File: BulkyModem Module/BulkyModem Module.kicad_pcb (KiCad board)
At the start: 2 copper layers, 100 x 100 mm, 81 parts, among them J1 DC IN, J2 DCE, J3 Module_Panel, J5 C64_Modem_IDC, K1 HK19F-DC, M1 Mounting, M2 Mounting, M3 Mounting, M4 Mounting, SW1 SET_1200, U1 74HCT244, U2 74HCT04, U3 MAX232, U4 MAX232, U5 74HCT04, U6 74HCT32

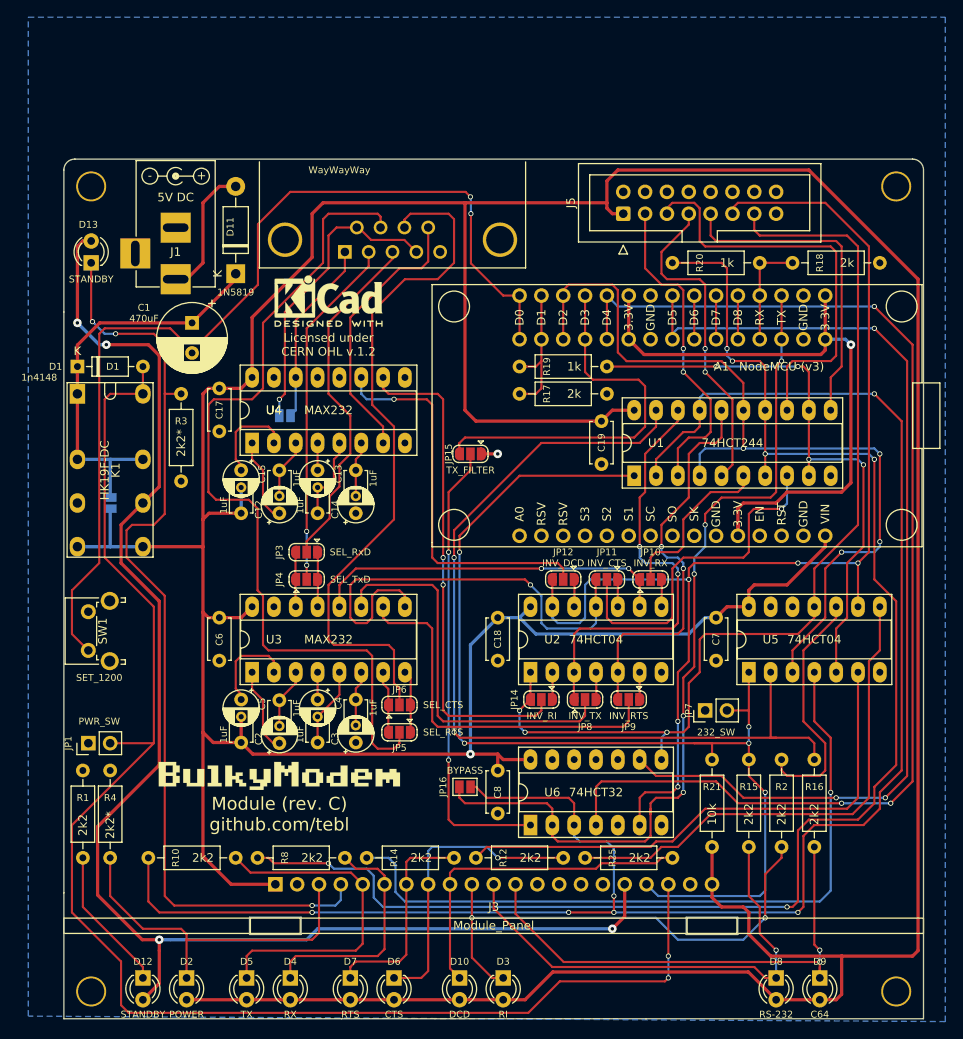
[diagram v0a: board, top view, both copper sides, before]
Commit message: Tweaks needed to make revision C actually work.
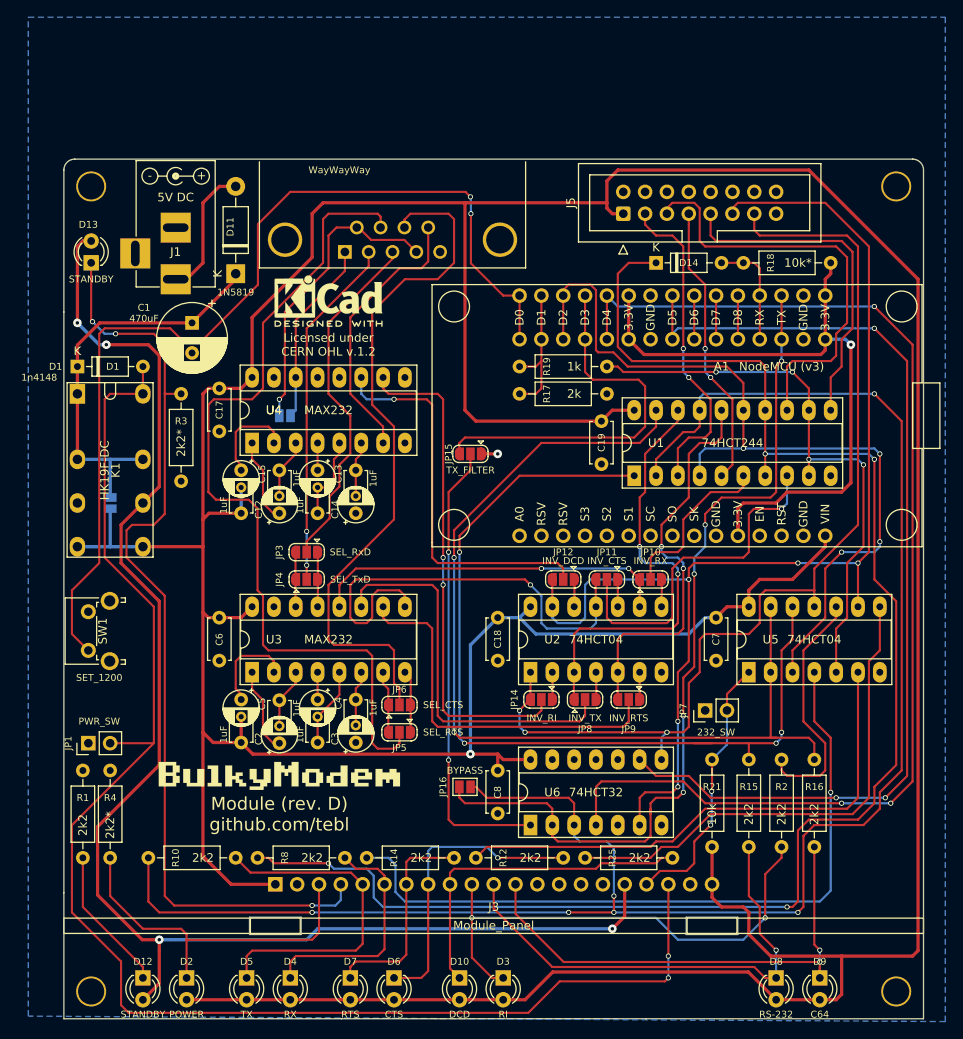
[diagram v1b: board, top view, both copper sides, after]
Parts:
- removed R20: 1k, resistor:R_Axial_DIN0207_L6.3mm_D2.5mm_P10.16mm_Horizontal
- added D14: 1N4148, Diode_THT:D_DO-35_SOD27_P7.62mm_Horizontal, F.Cu at (139.1, 66.7)
- R18: value 2k -> 10k*
- moved R18 5.72 mm to (159.4, 66.7)
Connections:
- J3 pad 18: MODE_232 -> MODE_SEL
- JP7 pad 2: MODE_232 -> MODE_SEL
- R18 pad 1: GND -> +3V3
- R21 pad 1: MODE_232 -> MODE_SEL
- U5 pad 1: MODE_232 -> MODE_SEL
- U5 pad 12: (no net) -> MODE_232
- U5 pad 13: GND -> MODE_C64
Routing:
- net MODE_SEL: track 0.00 -> 31.4 mm, vias 0 -> 2
- net MODE_232: track 128.1 -> 104.5 mm, vias 5 -> 4
- net ESP_RX: track 175.0 -> 184.8 mm, vias 6 -> 4
- net MODE_C64: track 106.5 -> 114.1 mm
- net /C64_RTS: track 38.0 -> 33.1 mm
- net +3V3: track 73.4 -> 77.4 mm
- net ESP_RI: track 116.3 -> 118.2 mm
- net /C64_CTS: track 37.9 -> 39.3 mm
- net /C64_RX: track 48.6 -> 50.0 mm
- net ESP_CTS: track 67.9 -> 66.8 mm
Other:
- board text added: "Module (rev. D) github.com/tebl"
- board text removed: "Module (rev. C) github.com/tebl"

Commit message: Upgrade to KiCAD8
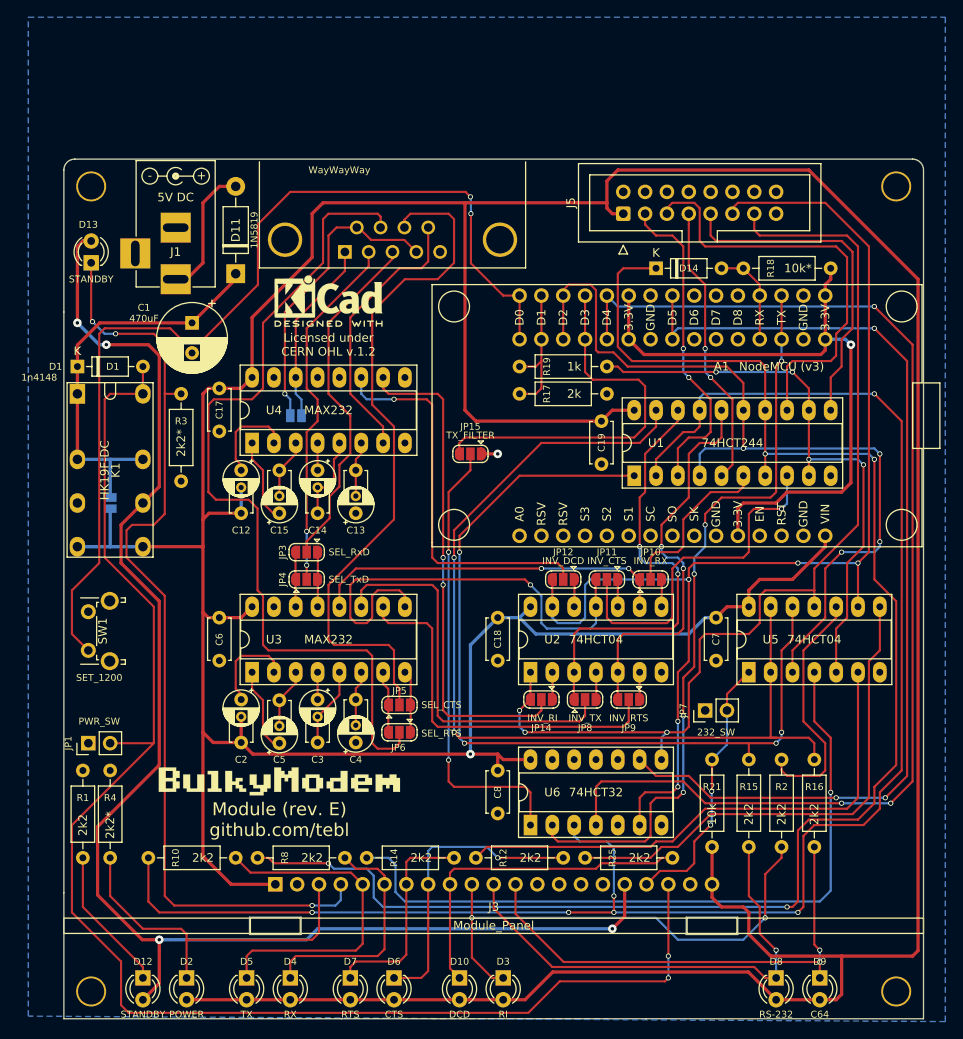
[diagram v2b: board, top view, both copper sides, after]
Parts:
- removed JP16: BYPASS, Jumper:SolderJumper-2_P1.3mm_Open_Pad1.0x1.5mm
- D11: footprint Diode_THT:D_DO-41_SOD81_P10.16mm_Horizontal -> BulkyModem:D_DO-41_SOD81_P10.16mm_Horizontal
- JP10, JP11, JP12, JP14, JP15, JP3, JP4, JP5, JP6, JP8, JP9: footprint Jumper:SolderJumper-3_P1.3mm_Open_RoundedPad1.0x1.5mm -> solder_bridge:SolderJumper-3_P1.3mm_Open_RoundedPad1.0x1.5mm
- JP13, JP2: footprint Jumper:SolderJumper-2_P1.3mm_Open_Pad1.0x1.5mm -> solder_bridge:SolderJumper-2_P1.3mm_Open_Pad1.0x1.5mm
- moved JP13 1.28 mm to (97.2, 84.5)
- moved D14 0.64 mm to (139.1, 67.3)
- moved G*** 0.64 mm to (95.2, 127.0)
- moved R18 0.64 mm to (159.4, 67.3)
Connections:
- net +3V3 renamed +3.3V
- net /ESP_DSR renamed /ESP_DSR_0
- net /ESP_DTR renamed /ESP_DTR_0
- A1 pad 1: (no net) -> unconnected-(A1-A0-Pad1)
- A1 pad 12: (no net) -> unconnected-(A1-EN-Pad12)
- A1 pad 13: (no net) -> unconnected-(A1-RST-Pad13)
- A1 pad 2: (no net) -> unconnected-(A1-RSV-Pad2)
- A1 pad 20: Net-(A1-Pad20) -> unconnected-(A1-D8-Pad20)_0
- A1 pad 3: (no net) -> unconnected-(A1-RSV-Pad3)
- A1 pad 4: (no net) -> unconnected-(A1-S3-Pad4)
- A1 pad 5: (no net) -> unconnected-(A1-S2-Pad5)
- A1 pad 6: (no net) -> unconnected-(A1-S1-Pad6)
- A1 pad 7: (no net) -> unconnected-(A1-SC-Pad7)
- A1 pad 8: (no net) -> unconnected-(A1-S0-Pad8)
- A1 pad 9: (no net) -> unconnected-(A1-SK-Pad9)
- C14 pad 1: Net-(C14-Pad1) -> unconnected-(U4-C2+-Pad4)
- C14 pad 2: Net-(C14-Pad2) -> unconnected-(U4-C2--Pad5)
- C15 pad 1: Net-(C15-Pad1) -> unconnected-(U4-C1+-Pad1)
- C15 pad 2: Net-(C15-Pad2) -> unconnected-(U4-C1--Pad3)
- C2 pad 1: Net-(C2-Pad1) -> unconnected-(U3-VS+-Pad2)
- C3 pad 1: Net-(C3-Pad1) -> unconnected-(U3-C2+-Pad4)
- C3 pad 2: Net-(C3-Pad2) -> unconnected-(U3-C2--Pad5)
- C4 pad 2: Net-(C4-Pad2) -> unconnected-(U3-VS--Pad6)
- C5 pad 1: Net-(C5-Pad1) -> unconnected-(U3-C1+-Pad1)
- C5 pad 2: Net-(C5-Pad2) -> unconnected-(U3-C1--Pad3)
- J5 pad 16: (no net) -> unconnected-(J5-N.C.-Pad16)
- J5 pad 8: (no net) -> unconnected-(J5-N.C-Pad8)
- K1 pad 6: (no net) -> unconnected-(K1-NC_1-Pad6)
- R12 pad 1: Net-(R12-Pad1) -> unconnected-(U5-Pad6)
- R14 pad 1: Net-(R14-Pad1) -> unconnected-(U5-Pad4)
- R2 pad 1: Net-(R2-Pad1) -> unconnected-(U5-Pad10)
- R25 pad 1: Net-(R25-Pad1) -> unconnected-(U5-Pad8)
- U3 pad 1: Net-(C5-Pad1) -> unconnected-(U3-C1+-Pad1)
- U3 pad 2: Net-(C2-Pad1) -> unconnected-(U3-VS+-Pad2)
- U3 pad 3: Net-(C5-Pad2) -> unconnected-(U3-C1--Pad3)
- U3 pad 4: Net-(C3-Pad1) -> unconnected-(U3-C2+-Pad4)
- U3 pad 5: Net-(C3-Pad2) -> unconnected-(U3-C2--Pad5)
- U3 pad 6: Net-(C4-Pad2) -> unconnected-(U3-VS--Pad6)
- U4 pad 1: Net-(C15-Pad1) -> unconnected-(U4-C1+-Pad1)
- U4 pad 12: (no net) -> unconnected-(U4-R1OUT-Pad12)
- U4 pad 3: Net-(C15-Pad2) -> unconnected-(U4-C1--Pad3)
- U4 pad 4: Net-(C14-Pad1) -> unconnected-(U4-C2+-Pad4)
- U4 pad 5: Net-(C14-Pad2) -> unconnected-(U4-C2--Pad5)
- U4 pad 9: (no net) -> unconnected-(U4-R2OUT-Pad9)
- U5 pad 10: Net-(R2-Pad1) -> unconnected-(U5-Pad10)
- U5 pad 4: Net-(R14-Pad1) -> unconnected-(U5-Pad4)
- U5 pad 6: Net-(R12-Pad1) -> unconnected-(U5-Pad6)
- U5 pad 8: Net-(R25-Pad1) -> unconnected-(U5-Pad8)
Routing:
- net Net-(R14-Pad1): track 84.7 -> 0.00 mm, vias 1 -> 0
- net unconnected-(U5-Pad4): track 0.00 -> 84.7 mm, vias 0 -> 1
- net unconnected-(U5-Pad6): track 0.00 -> 61.9 mm
- net Net-(R12-Pad1): track 61.9 -> 0.00 mm
- net Net-(R25-Pad1): track 58.7 -> 0.00 mm
- net unconnected-(U5-Pad8): track 0.00 -> 58.7 mm
- net unconnected-(U5-Pad10): track 0.00 -> 28.6 mm
- net Net-(R2-Pad1): track 28.6 -> 0.00 mm
- net Net-(A1-TX): track 103.0 -> 87.2 mm
- net ESP_TX: track 212.8 -> 197.4 mm
- net unconnected-(U3-VS+-Pad2): track 0.00 -> 10.9 mm
- net Net-(C2-Pad1): track 10.9 -> 0.00 mm
- net unconnected-(U4-C2--Pad5): track 0.00 -> 9.94 mm
- net Net-(C14-Pad2): track 9.94 -> 0.00 mm
- net Net-(C15-Pad1): track 9.91 -> 0.00 mm
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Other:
- net class Default removed
- net class Power removed
- board text added: "Module (rev. E) github.com/tebl"
- board text removed: "Module (rev. D) github.com/tebl"

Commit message: Add mounting points for audio module
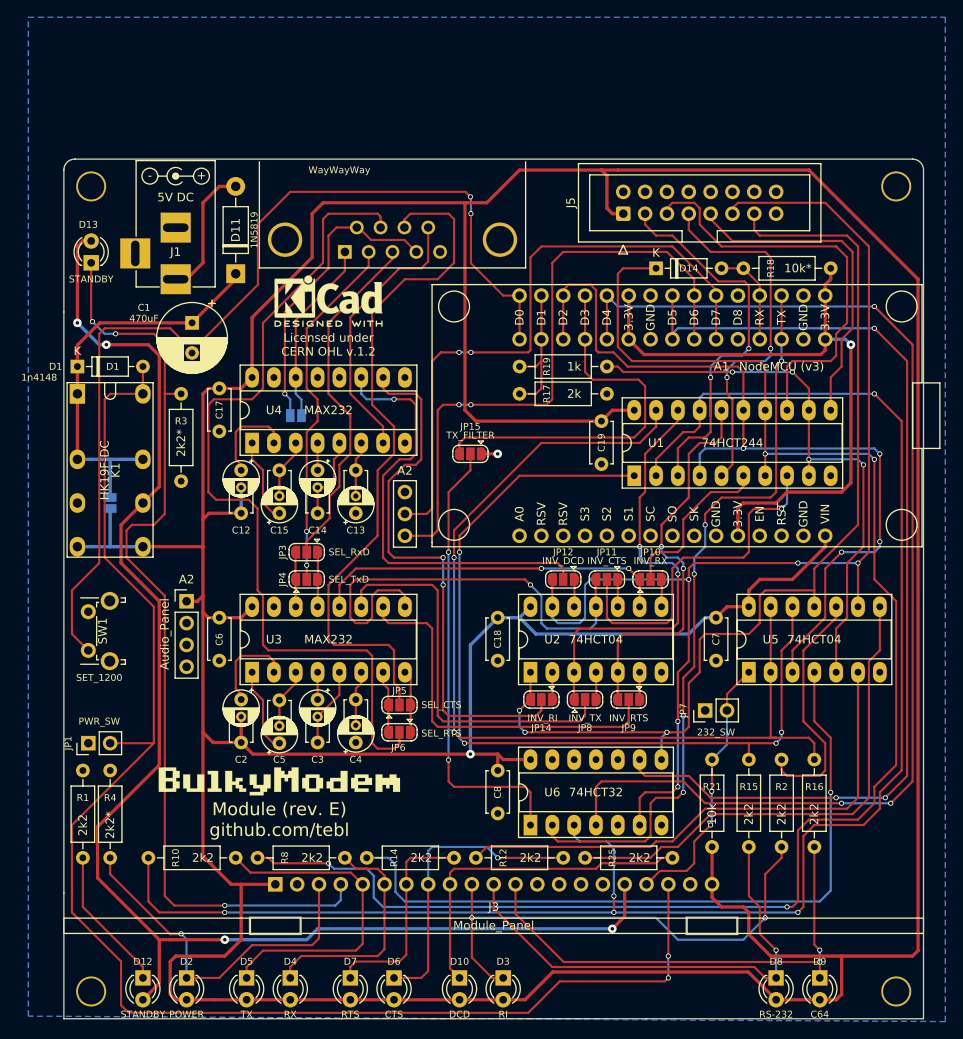
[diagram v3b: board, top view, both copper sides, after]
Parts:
- added A2: Audio_Panel, BulkyModem:AudioModule, F.Cu at (109.9, 93.3)
- M1, M2, M3, M4: footprint mounting:M3 -> mounting:M3_pin
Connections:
- net /Front panel/LED_C64 renamed /Front Panel/LED_C64
- net /Front panel/LED_CTS renamed /Front Panel/LED_CTS
- net /Front panel/LED_DCD renamed /Front Panel/LED_DCD
- net /Front panel/LED_POW renamed /Front Panel/LED_POW
- net /Front panel/LED_RI renamed /Front Panel/LED_RI
- net /Front panel/LED_RS232 renamed /Front Panel/LED_RS232
- net /Front panel/LED_RTS renamed /Front Panel/LED_RTS
- net /Front panel/LED_RX renamed /Front Panel/LED_RX
- net /Front panel/LED_STB renamed /Front Panel/LED_STB
- net /Front panel/LED_TX renamed /Front Panel/LED_TX
- A1 pad 21: /ESP_DSR_0 -> AUDIO_TX
- A1 pad 22: /ESP_DTR_0 -> AUDIO_RX
- J3 pad 13: (no net) -> unconnected-(J3-N.C.-Pad13)
- J3 pad 14: (no net) -> unconnected-(J3-N.C.-Pad14)
- J3 pad 15: (no net) -> unconnected-(J3-N.C.-Pad15)
- J3 pad 16: (no net) -> unconnected-(J3-N.C.-Pad16)
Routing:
- net AUDIO_TX: track 0.00 -> 73.3 mm, vias 0 -> 2
- net AUDIO_RX: track 0.00 -> 73.1 mm, vias 0 -> 2
- net +5V: track 557.2 -> 583.7 mm
- net /C64_TX: track 37.4 -> 48.3 mm
- net /C64_RTS: track 33.1 -> 43.0 mm
- net Net-(JP12-C): track 45.5 -> 51.6 mm
- net Net-(JP14-C): track 58.2 -> 64.0 mm
- net VSB: track 167.4 -> 166.2 mm
- net /C64_CTS: track 39.3 -> 38.2 mm
- net /C64_RX: track 50.0 -> 48.9 mm
- net Net-(A1-D5): track 117.1 -> 117.9 mm
- net /Front Panel/LED_TX: track 39.6 -> 38.9 mm
- net ESP_RTS: track 99.2 -> 100.0 mm
- net /Front Panel/LED_POW: track 41.6 -> 42.1 mm, vias 0 -> 1
- net ESP_TX: vias 6 -> 5
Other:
- board text added: "A2"

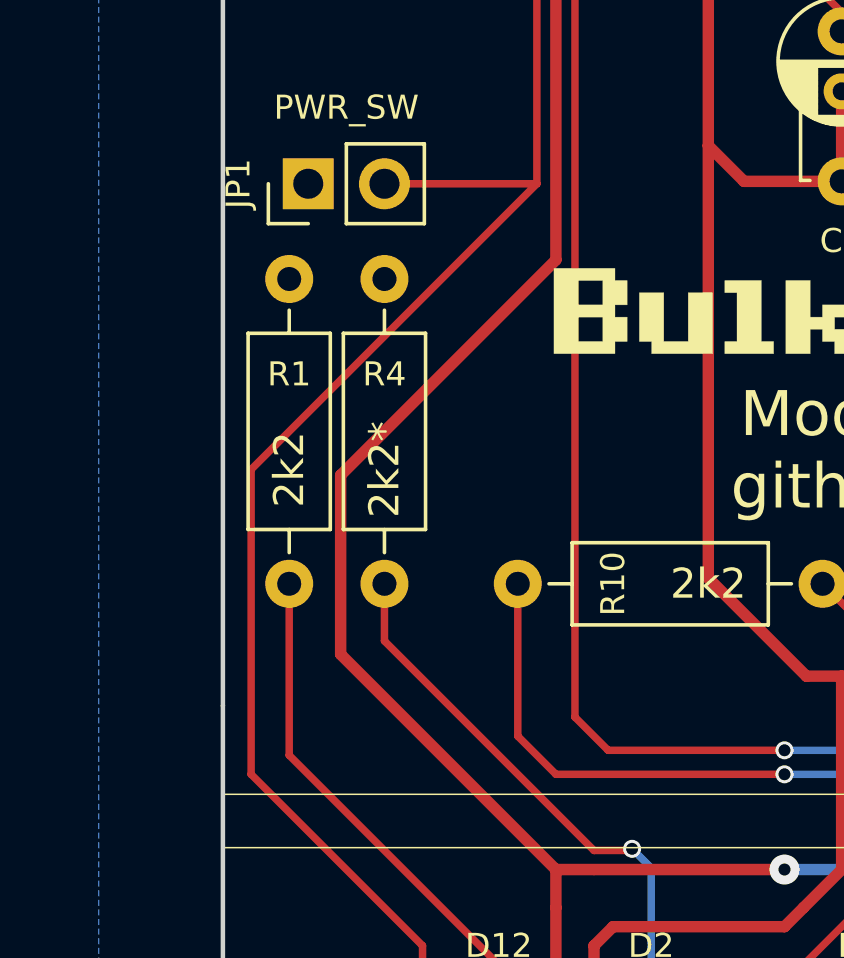
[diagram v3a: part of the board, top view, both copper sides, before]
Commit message: Change some resistor values
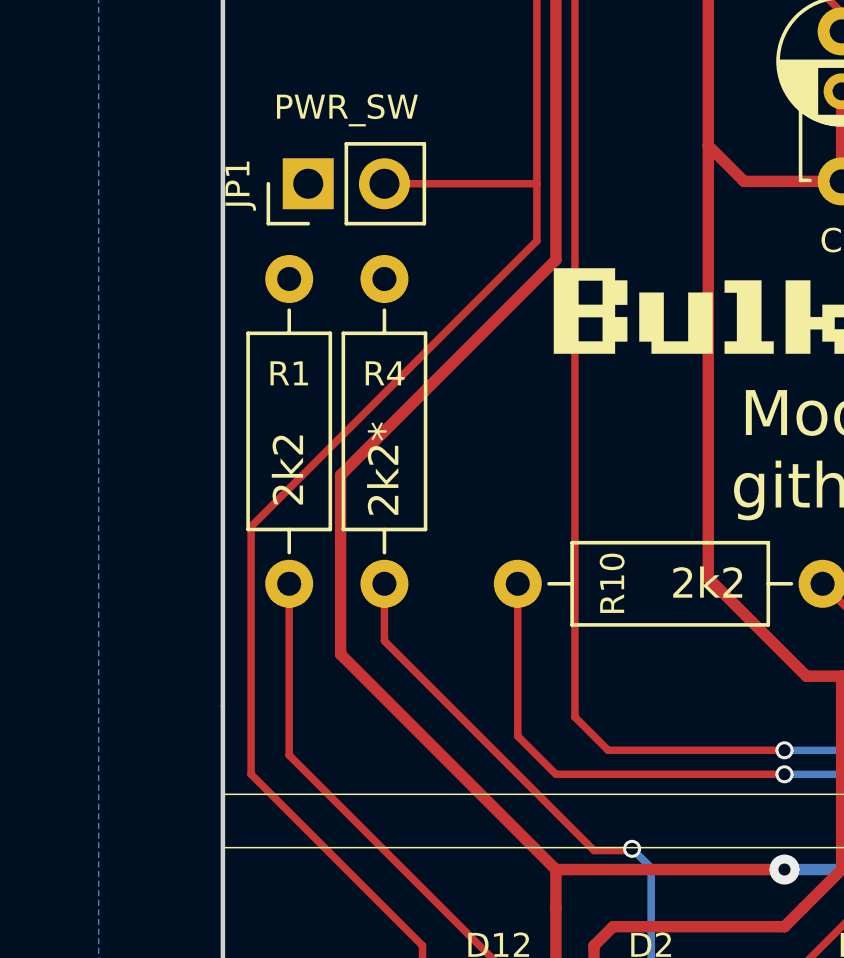
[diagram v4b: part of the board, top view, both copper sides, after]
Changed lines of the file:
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@@
 	)
 	(segment
-		(start 71.12 142.24)
-		(end 71.12 132.08)
+		(start 76.835 147.955)
+		(end 71.12 142.24)
+		(width 0.25)
+		(layer "F.Cu")
+		(net 18)
+	)
+	(segment
+		(start 75.565 81.915)
+		(end 79.375 81.915)
+		(width 0.25)
+		(layer "F.Cu")
+		(net 18)
+	)
+	(segment
+		(start 80.645 124.46)
+		(end 80.645 122.555)
+		(width 0.25)
+		(layer "F.Cu")
+		(net 18)
+	)
+	(segment
+		(start 124.206 153.924)
+		(end 77.724 153.924)
+		(width 0.25)
+		(layer "F.Cu")
+		(net 18)
+	)
+	(segment
+		(start 140.5 138.97)
+		(end 140.5 147.32)
+		(width 0.25)
+		(layer "F.Cu")
+		(net 18)
+	)
+	(segment
+		(start 76.835 153.035)
+		(end 76.835 147.955)
 		(width 0.25)
 		(layer "F.Cu")
@@
 	)
 	(segment
-		(start 124.206 153.924)
-		(end 77.724 153.924)
-		(width 0.25)
-		(layer "F.Cu")
-		(net 18)
-	)
-	(segment
-		(start 75.565 81.915)
-		(end 79.375 81.915)
-		(width 0.25)
-		(layer "F.Cu")
-		(net 18)
-	)
-	(segment
-		(start 140.5 138.97)
-		(end 140.5 147.32)
-		(width 0.25)
-		(layer "F.Cu")
-		(net 18)
-	)
-	(segment
 		(start 74.93 82.55)
 		(end 75.565 81.915)
@@
 	)
 	(segment
-		(start 76.835 153.035)
-		(end 76.835 147.955)
+		(start 77.724 153.924)
+		(end 76.835 153.035)
 		(width 0.25)
 		(layer "F.Cu")
@@
 	)
 	(segment
-		(start 77.724 153.924)
-		(end 76.835 153.035)
+		(start 71.12 133.985)
+		(end 80.645 124.46)
+		(width 0.25)
+		(layer "F.Cu")
+		(net 18)
+	)
+	(segment
+		(start 71.12 142.24)
+		(end 71.12 133.985)
+		(width 0.25)
+		(layer "F.Cu")
+		(net 18)
+	)
+	(segment
+		(start 127.87 150.26)
+		(end 124.206 153.924)
 		(width 0.25)
 		(layer "F.Cu")
@@
 	)
 	(segment
-		(start 76.835 147.955)
-		(end 71.12 142.24)
-		(width 0.25)
-		(layer "F.Cu")
-		(net 18)
-	)
-	(segment
-		(start 71.12 132.08)
-		(end 80.645 122.555)
-		(width 0.25)
-		(layer "F.Cu")
-		(net 18)
-	)
-	(segment
-		(start 127.87 150.26)
-		(end 124.206 153.924)
+		(start 140.5 149.86)
+		(end 140.1 150.26)
 		(width 0.25)
 		(layer "F.Cu")
@@
 		(width 0.25)
 		(layer "F.Cu")
-		(net 18)
-	)
-	(segment
-		(start 140.5 149.86)
-		(end 140.1 150.26)
-		(width 0.25)
-		(layer "F.Cu")
